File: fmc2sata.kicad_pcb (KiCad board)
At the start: 4 copper layers, 108 x 69 mm, 61 parts, among them J1 ASP-134488-01, J2 1-2199230-6, J3 te-770829-1, Q1 BSS138APW, Q2 BSS138APW, Q3 DMG2305UX-13, Q4 BSS138APW, U1 TPS565208, U2 TPS565208, Y1 AX3DAF1-150.0000

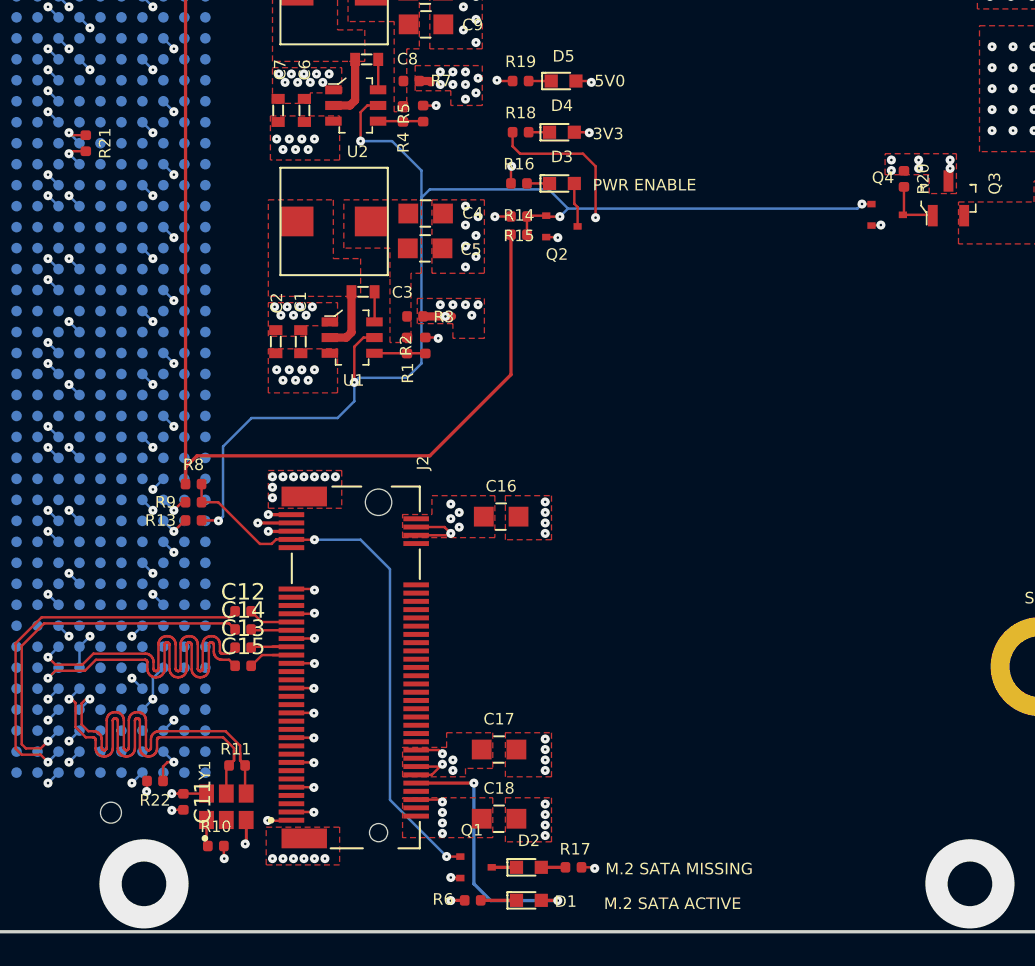
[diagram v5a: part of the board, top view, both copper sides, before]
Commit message: Update designators, DRC clean
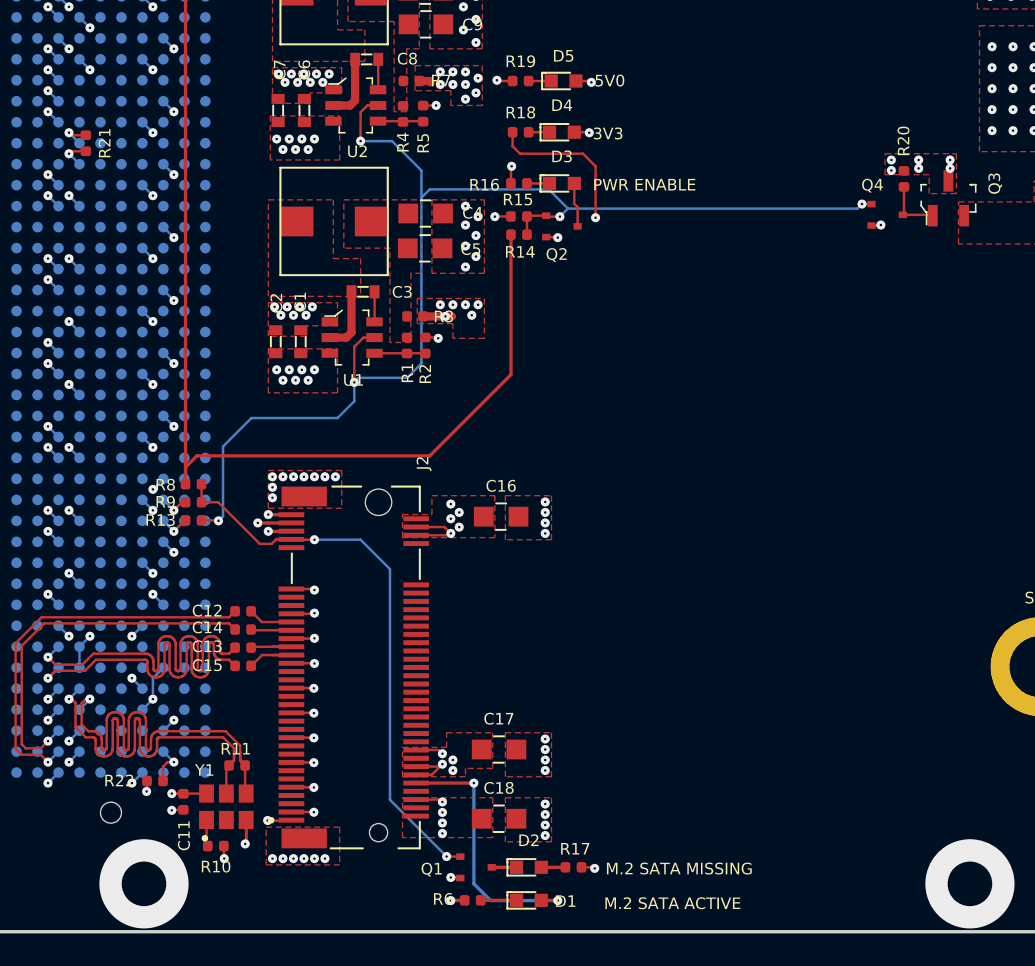
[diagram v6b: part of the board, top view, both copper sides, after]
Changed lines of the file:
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@@
   (layers
     (0 F.Cu signal)
-    (1 In1.Cu signal hide)
-    (2 In2.Cu signal hide)
-    (31 B.Cu signal)
+    (1 In1.Cu signal)
+    (2 In2.Cu signal)
+    (31 B.Cu signal hide)
     (32 B.Adhes user hide)
     (33 F.Adhes user hide)
@@
     (35 F.Paste user hide)
     (36 B.SilkS user hide)
-    (37 F.SilkS user hide)
+    (37 F.SilkS user)
     (38 B.Mask user hide)
     (39 F.Mask user)
@@
     (tags resistor)
     (attr smd)
-    (fp_text reference R20 (at 0 -1.17 90) (layer F.SilkS)
+    (fp_text reference R20 (at -2.286 0 90) (layer F.SilkS)
       (effects (font (size 0.7 0.7) (thickness 0.15)))
     )
@@
     )
     (fp_text user %R (at 0 0 90) (layer F.Fab)
-      (effects (font (size 0.25 0.25) (thickness 0.04)))
+      (effects (font (size 0.7 0.7) (thickness 0.15)))
     )
     (fp_line (start -0.5 0.25) (end -0.5 -0.25) (layer F.Fab) (width 0.1))
@@
     (tags resistor)
     (attr smd)
-    (fp_text reference R16 (at 0 -1.17) (layer F.SilkS)
+    (fp_text reference R16 (at -2.094 0.105) (layer F.SilkS)
       (effects (font (size 0.7 0.7) (thickness 0.15)))
     )
@@
     )
     (fp_text user %R (at 0 0) (layer F.Fab)
-      (effects (font (size 0.25 0.25) (thickness 0.04)))
+      (effects (font (size 0.7 0.7) (thickness 0.15)))
     )
     (fp_line (start -0.5 0.25) (end -0.5 -0.25) (layer F.Fab) (width 0.1))
@@
     (tags resistor)
     (attr smd)
-    (fp_text reference R15 (at 0 -1.17) (layer F.SilkS)
+    (fp_text reference R15 (at 0.062 1.006) (layer F.SilkS)
       (effects (font (size 0.7 0.7) (thickness 0.15)))
     )
@@
     )
     (fp_text user %R (at 0 0) (layer F.Fab)
-      (effects (font (size 0.25 0.25) (thickness 0.04)))
+      (effects (font (size 0.7 0.7) (thickness 0.15)))
     )
     (fp_line (start -0.5 0.25) (end -0.5 -0.25) (layer F.Fab) (width 0.1))
@@
     (tags resistor)
     (attr smd)
-    (fp_text reference R14 (at 0 -1.17) (layer F.SilkS)
+    (fp_text reference R14 (at 0.065 1.069) (layer F.SilkS)
       (effects (font (size 0.7 0.7) (thickness 0.15)))
     )
@@
     )
     (fp_text user %R (at 0 0) (layer F.Fab)
-      (effects (font (size 0.25 0.25) (thickness 0.04)))
+      (effects (font (size 0.7 0.7) (thickness 0.15)))
     )
     (fp_line (start -0.5 0.25) (end -0.5 -0.25) (layer F.Fab) (width 0.1))
@@
     (tags resistor)
     (attr smd)
-    (fp_text reference R10 (at 0 -1.17) (layer F.SilkS)
+    (fp_text reference R10 (at 0 1.27) (layer F.SilkS)
       (effects (font (size 0.7 0.7) (thickness 0.15)))
     )
@@
     )
     (fp_text user %R (at 0 0) (layer F.Fab)
-      (effects (font (size 0.25 0.25) (thickness 0.04)))
+      (effects (font (size 0.7 0.7) (thickness 0.15)))
     )
     (fp_line (start -0.5 0.25) (end -0.5 -0.25) (layer F.Fab) (width 0.1))
@@
     (tags resistor)
     (attr smd)
-    (fp_text reference R8 (at 0 -1.17) (layer F.SilkS)
+    (fp_text reference R8 (at -1.698 0.066) (layer F.SilkS)
       (effects (font (size 0.7 0.7) (thickness 0.15)))
     )
@@
     )
     (fp_text user %R (at 0 0) (layer F.Fab)
-      (effects (font (size 0.25 0.25) (thickness 0.04)))
+      (effects (font (size 0.7 0.7) (thickness 0.15)))
     )
     (fp_line (start -0.5 0.25) (end -0.5 -0.25) (layer F.Fab) (width 0.1))
@@
     (tags resistor)
     (attr smd)
-    (fp_text reference R5 (at 0 -1.17 90) (layer F.SilkS)
+    (fp_text reference R5 (at -1.795 0.023 90) (layer F.SilkS)
       (effects (font (size 0.7 0.7) (thickness 0.15)))
     )
@@
     )
     (fp_text user %R (at 0 0 90) (layer F.Fab)
-      (effects (font (size 0.25 0.25) (thickness 0.04)))
+      (effects (font (size 0.7 0.7) (thickness 0.15)))
     )
     (fp_line (start -0.5 0.25) (end -0.5 -0.25) (layer F.Fab) (width 0.1))
@@
     (tags resistor)
     (attr smd)
-    (fp_text reference R2 (at 0 -1.17 90) (layer F.SilkS)
+    (fp_text reference R2 (at -1.725 0.02 90) (layer F.SilkS)
       (effects (font (size 0.7 0.7) (thickness 0.15)))
     )
@@
     )
     (fp_text user %R (at 0 0 90) (layer F.Fab)
-      (effects (font (size 0.25 0.25) (thickness 0.04)))
+      (effects (font (size 0.7 0.7) (thickness 0.15)))
     )
     (fp_line (start -0.5 0.25) (end -0.5 -0.25) (layer F.Fab) (width 0.1))
@@
     (tags resistor)
     (attr smd)
-    (fp_text reference C15 (at 0 -1.17) (layer F.SilkS)
-      (effects (font (size 1 1) (thickness 0.15)))
+    (fp_text reference C15 (at -2.158 -0.012) (layer F.SilkS)
+      (effects (font (size 0.7 0.7) (thickness 0.15)))
     )
     (fp_text value C_10n_0402 (at 0 1.17) (layer F.Fab)
@@
     )
     (fp_text user %R (at 0 0) (layer F.Fab)
-      (effects (font (size 0.25 0.25) (thickness 0.04)))
+      (effects (font (size 0.7 0.7) (thickness 0.15)))
     )
     (fp_line (start 0.93 0.47) (end -0.93 0.47) (layer F.CrtYd) (width 0.05))
@@
     (tags resistor)
     (attr smd)
-    (fp_text reference C14 (at 0 -1.17) (layer F.SilkS)
-      (effects (font (size 1 1) (thickness 0.15)))
+    (fp_text reference C14 (at -2.158 -0.098) (layer F.SilkS)
+      (effects (font (size 0.7 0.7) (thickness 0.15)))
     )
     (fp_text value C_10n_0402 (at 0 1.17) (layer F.Fab)
@@
     )
     (fp_text user %R (at 0 0) (layer F.Fab)
-      (effects (font (size 0.25 0.25) (thickness 0.04)))
+      (effects (font (size 0.7 0.7) (thickness 0.15)))
     )
     (fp_line (start 0.93 0.47) (end -0.93 0.47) (layer F.CrtYd) (width 0.05))
@@
     (tags resistor)
     (attr smd)
-    (fp_text reference C13 (at 0 -1.17) (layer F.SilkS)
-      (effects (font (size 1 1) (thickness 0.15)))
+    (fp_text reference C13 (at -2.158 -0.055) (layer F.SilkS)
+      (effects (font (size 0.7 0.7) (thickness 0.15)))
     )
     (fp_text value C_10n_0402 (at 0 1.17) (layer F.Fab)
@@
     )
     (fp_text user %R (at 0 0) (layer F.Fab)
-      (effects (font (size 0.25 0.25) (thickness 0.04)))
+      (effects (font (size 0.7 0.7) (thickness 0.15)))
     )
     (fp_line (start 0.93 0.47) (end -0.93 0.47) (layer F.CrtYd) (width 0.05))
@@
     (tags resistor)
     (attr smd)
-    (fp_text reference C12 (at 0 -1.17) (layer F.SilkS)
-      (effects (font (size 1 1) (thickness 0.15)))
+    (fp_text reference C12 (at -2.158 -0.014) (layer F.SilkS)
+      (effects (font (size 0.7 0.7) (thickness 0.15)))
     )
     (fp_text value C_10n_0402 (at 0 1.17) (layer F.Fab)
@@
     )
     (fp_text user %R (at 0 0) (layer F.Fab)
-      (effects (font (size 0.25 0.25) (thickness 0.04)))
+      (effects (font (size 0.7 0.7) (thickness 0.15)))
     )
     (fp_line (start 0.93 0.47) (end -0.93 0.47) (layer F.CrtYd) (width 0.05))
@@
     (tags resistor)
     (attr smd)
-    (fp_text reference C11 (at 0 -1.17 90) (layer F.SilkS)
-      (effects (font (size 1 1) (thickness 0.15)))
+    (fp_text reference C11 (at 2.041 -0.06 90) (layer F.SilkS)
+      (effects (font (size 0.7 0.7) (thickness 0.15)))
     )
     (fp_text value C_100n_0402 (at 0 1.17 90) (layer F.Fab)
@@
     )
     (fp_text user %R (at 0 0 90) (layer F.Fab)
-      (effects (font (size 0.25 0.25) (thickness 0.04)))
+      (effects (font (size 0.7 0.7) (thickness 0.15)))
     )
     (fp_line (start 0.93 0.47) (end -0.93 0.47) (layer F.CrtYd) (width 0.05))
@@
     (tags resistor)
     (attr smd)
-    (fp_text reference R22 (at 0 -1.17) (layer F.SilkS)
+    (fp_text reference R22 (at 2.159 0) (layer F.SilkS)
       (effects (font (size 0.7 0.7) (thickness 0.15)))
     )
@@
     (at 127.59 68.6)
     (attr smd)
-    (fp_text reference Q4 (at -0.25 -2.25) (layer F.SilkS)
+    (fp_text reference Q4 (at -0.889 -1.795) (layer F.SilkS)
       (effects (font (size 0.7 0.7) (thickness 0.15)))
     )
@@
     (at 102.7 108.1)
     (attr smd)
-    (fp_text reference Q1 (at -0.25 -2.25) (layer F.SilkS)
+    (fp_text reference Q1 (at -2.669 0.107) (layer F.SilkS)
       (effects (font (size 0.7 0.7) (thickness 0.15)))
     )
@@
   (module fmc2sata-footprints:AX3DAF1 (layer F.Cu)
     (at 87.585 104.434)
-    (fp_text reference Y1 (at -1.3 -2.2 90) (layer F.SilkS)
+    (fp_text reference Y1 (at -1.3 -2.2 180) (layer F.SilkS)
       (effects (font (size 0.7 0.7) (thickness 0.15)))
     )
@@
       )
     )
+  )
+  (zone (net 0) (net_name "") (layers In1.Cu In2.Cu) (hatch edge 0.508)
+    (connect_pads yes (clearance 0.25))
+    (min_thickness 0.254)
+    (keepout (tracks not_allowed) (vias not_allowed) (copperpour not_allowed))
+    (fill (arc_segments 32) (thermal_gap 0.508) (thermal_bridge_width 0.508))
+    (polygon
+      (pts
+        (xy 89.363 96.396) (xy 87.839 96.396) (xy 87.839 91.824) (xy 89.363 91.824)
+      )
+    )

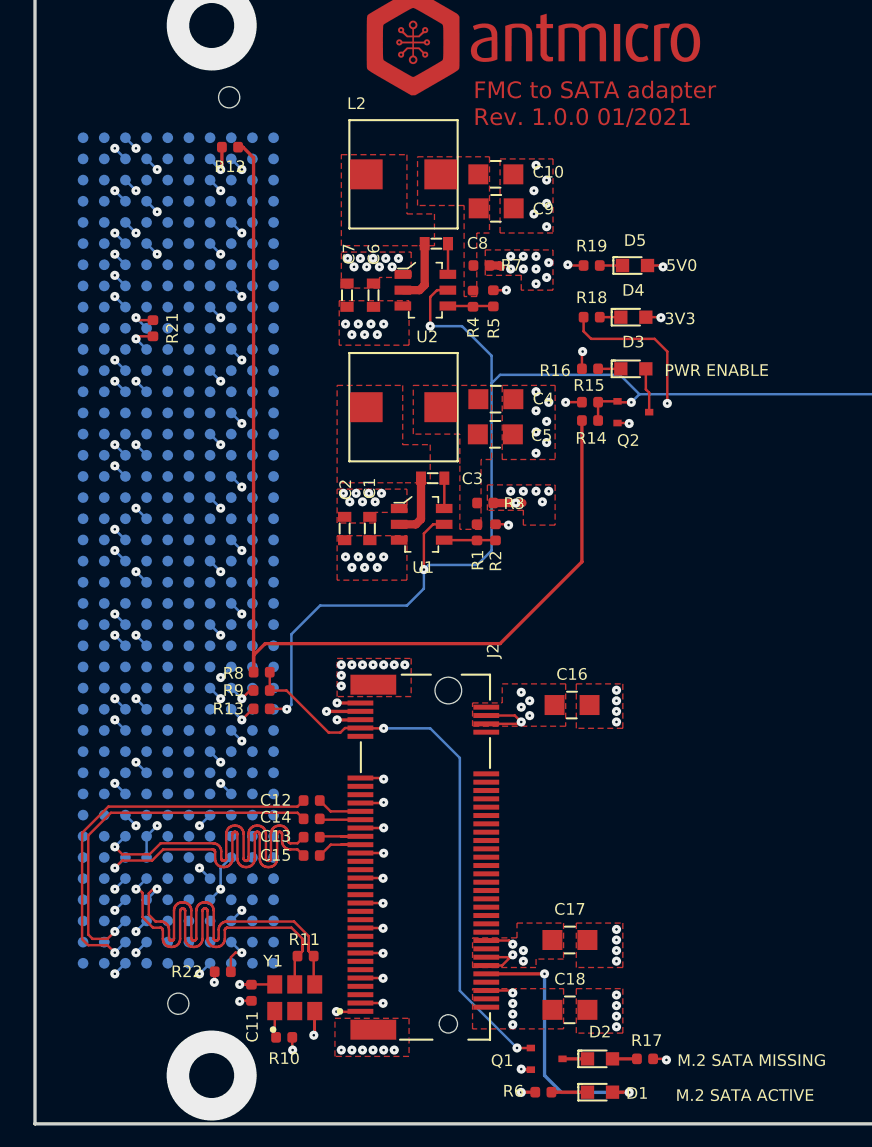
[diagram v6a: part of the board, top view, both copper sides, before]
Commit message: Update layout, DRC clean
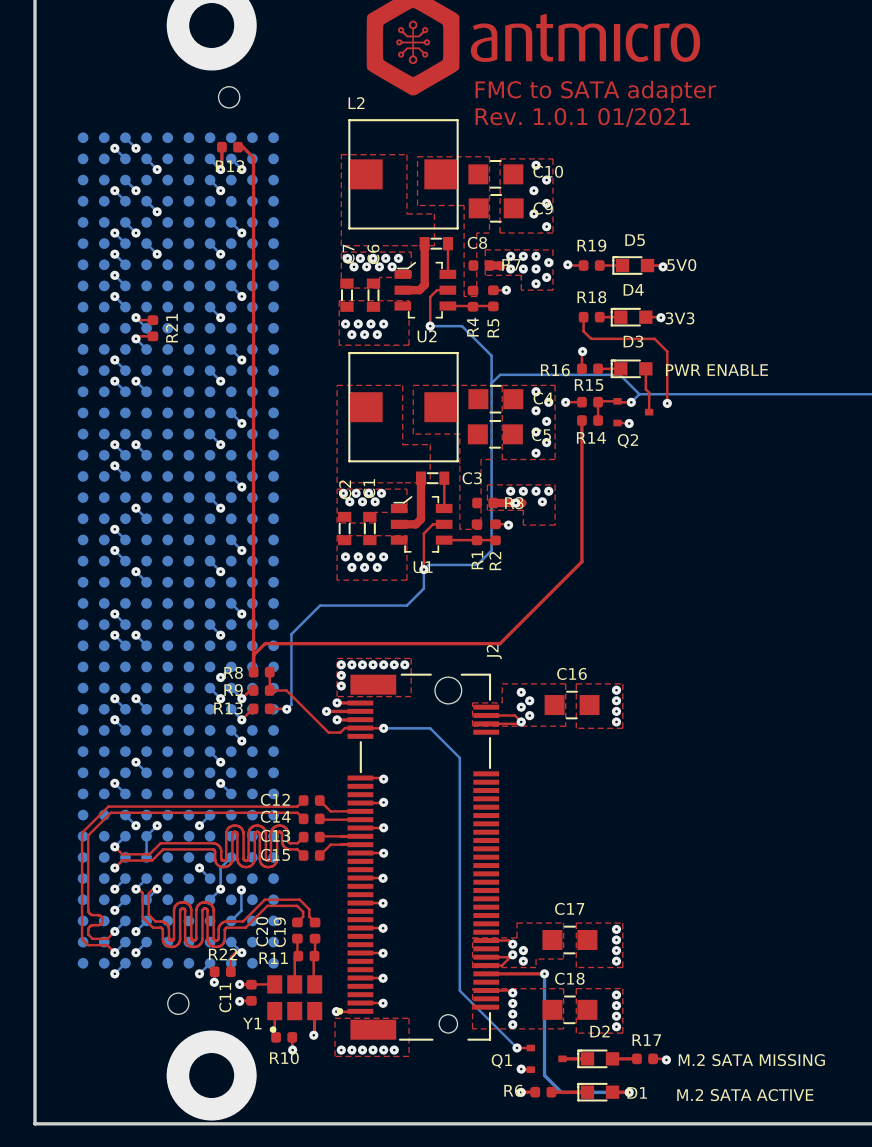
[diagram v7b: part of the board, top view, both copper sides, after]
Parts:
- added C19: C_100n_0402, antmicro-footprints:0402-cap, F.Cu at (88.8, 100.4)
- added C20: C_100n_0402, antmicro-footprints:0402-cap, F.Cu at (87.7, 100.4)
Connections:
- J1 pad C39: +12V -> Net-(J1-PadC39)
- R11 pad 1: SATA_CLK_P -> Net-(C19-Pad2)
- R11 pad 2: SATA_CLK_N -> Net-(C20-Pad2)
- Y1 pad 4: SATA_CLK_P -> Net-(C19-Pad2)
- Y1 pad 5: SATA_CLK_N -> Net-(C20-Pad2)
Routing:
- net Net-(C19-Pad2): track 0.00 -> 2.83 mm
- net Net-(C20-Pad2): track 0.00 -> 2.82 mm
- net SATA_CLK_P: track 26.7 -> 24.2 mm
- net SATA_CLK_N: track 26.4 -> 24.1 mm
- net SATA_A_N: track 22.4 -> 23.6 mm
- net GND: track 88.0 -> 89.2 mm
- net +12V: track 3.75 -> 2.85 mm, vias 24 -> 23
- net Net-(J1-PadC39): track 0.00 -> 0.90 mm, vias 0 -> 1
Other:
- board text added: "FMC to SATA adapter Rev. 1.0.1 01/2021"
- board text removed: "FMC to SATA adapter Rev. 1.0.0 01/2021"
